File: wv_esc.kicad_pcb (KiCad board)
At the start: 2 copper layers, 81 x 49 mm, 40 parts, among them J1 Conn_01x02, J3 Conn_01x03, Q1 IRF135B203, Q2 IRF135B203, Q3 IRF135B203, Q4 IRF135B203, Q5 IRF135B203, Q6 IRF135B203, Q7 AS78LXX, U1 ATtiny404-SS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

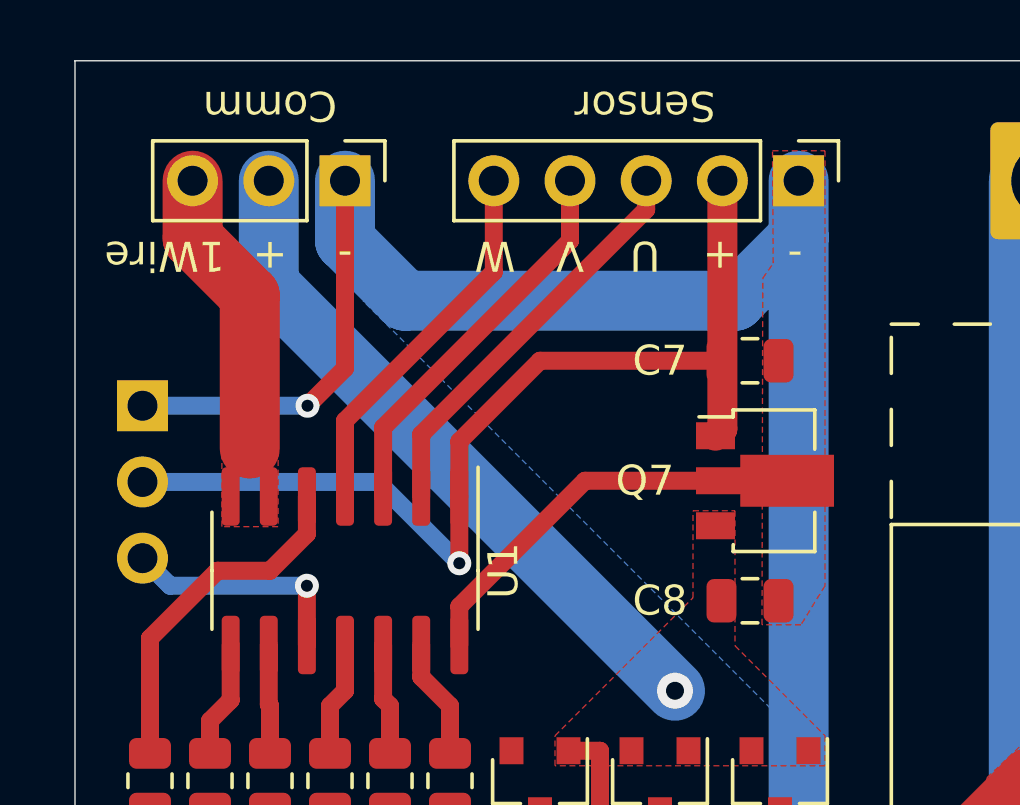
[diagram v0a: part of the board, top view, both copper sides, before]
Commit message: use sheet for 5V regulator
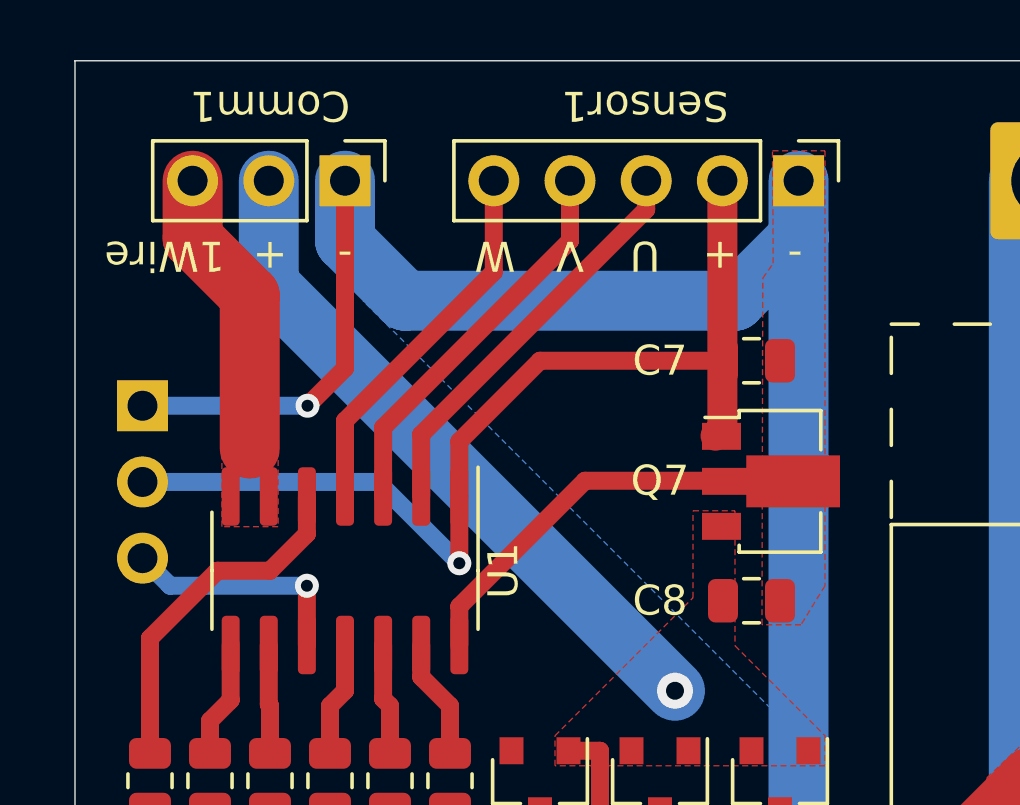
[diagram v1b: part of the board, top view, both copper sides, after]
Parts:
- C6: value 2200μF, 100V -> 220μF, 100V
- U1: value ATtiny404-SS -> ATtiny204-SS
- moved Q7 0.20 mm to (67.2, 48.0)
- turned C7 to 180 degrees
- renumbered Comm to Comm1, Debug to Debug1, Sensor to Sensor1
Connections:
- net +15V renamed 14V
- C7 pad 1: +5V -> GND
- C7 pad 2: GND -> +5V
